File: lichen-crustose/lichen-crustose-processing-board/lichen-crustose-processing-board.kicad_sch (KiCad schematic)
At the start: 3 parts

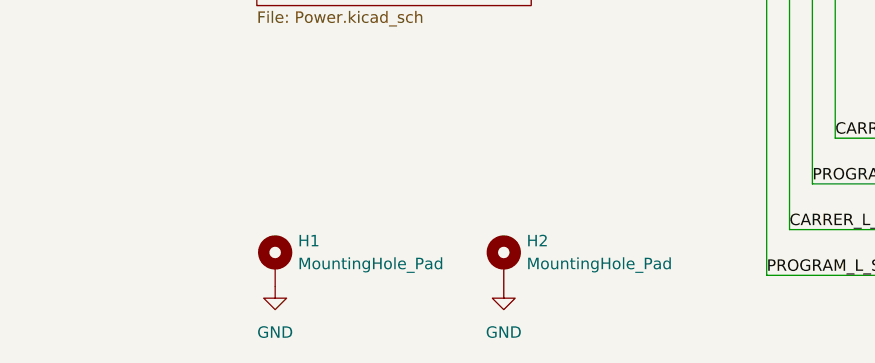
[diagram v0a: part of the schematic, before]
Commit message: Updates Lichen symbols and footprints. Fixes to Crustose and Vactrol VCA. Adds 3D model of the RP2350 dual USB board.
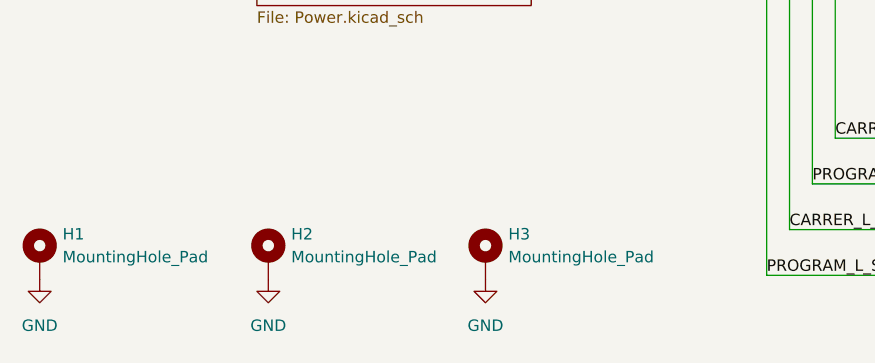
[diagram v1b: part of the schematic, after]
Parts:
- added H3: MountingHole_Pad, MountingHole:MountingHole_2.2mm_M2_Pad, symbol Mechanical:MountingHole_Pad
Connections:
- net GND: now also H3.1
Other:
- moved on the sheet: H1, H2
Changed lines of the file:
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@@
 	(symbol
 		(lib_id "power:GND")
-		(at 113.792 135.382 0)
+		(at 111.76 134.62 0)
 		(mirror y)
 		(unit 1)
@@
 		(dnp no)
 		(fields_autoplaced yes)
+		(property "Reference" "#PWR020"
+			(at 111.76 140.97 0)
+			(effects
+				(font
+					(size 1.27 1.27)
+				)
+				(hide yes)
+			)
+		)
+		(property "Value" "GND"
+			(at 111.76 139.7 0)
+			(effects
+				(font
+					(size 1.27 1.27)
+				)
+			)
+		)
+		(property "Footprint" ""
+			(at 111.76 134.62 0)
+			(effects
+				(font
+					(size 1.27 1.27)
+				)
+				(hide yes)
+			)
+		)
+		(property "Datasheet" ""
+			(at 111.76 134.62 0)
+			(effects
+				(font
+					(size 1.27 1.27)
+				)
+				(hide yes)
+			)
+		)
+		(property "Description" "Power symbol creates a global label with name \"GND\" , ground"
+			(at 111.76 134.62 0)
+			(effects
+				(font
+					(size 1.27 1.27)
+				)
+				(hide yes)
+			)
+		)
+		(pin "1"
+		)
+		(instances
+			(project "lichen-crustose-processing-board"
+				(path "/c32352bf-fefd-4f63-8ef8-68bcf6fd3821"
+					(reference "#PWR020")
+					(unit 1)
+				)
+			)
+		)
+	)
+	(symbol
+		(lib_id "power:GND")
+		(at 87.63 134.62 0)
+		(mirror y)
+		(unit 1)
+		(exclude_from_sim no)
+		(in_bom yes)
+		(on_board yes)
+		(dnp no)
+		(fields_autoplaced yes)
 		(property "Reference" "#PWR02"
-			(at 113.792 141.732 0)
+			(at 87.63 140.97 0)
 			(effects
 				(font
@@
 		)
 		(property "Value" "GND"
-			(at 113.792 140.462 0)
+			(at 87.63 139.7 0)
 			(effects
 				(font
@@
 		)
 		(property "Footprint" ""
-			(at 113.792 135.382 0)
+			(at 87.63 134.62 0)
 			(effects
 				(font
@@
 		)
 		(property "Datasheet" ""
-			(at 113.792 135.382 0)
+			(at 87.63 134.62 0)
 			(effects
 				(font
@@
 		)
 		(property "Description" "Power symbol creates a global label with name \"GND\" , ground"
-			(at 113.792 135.382 0)
+			(at 87.63 134.62 0)
 			(effects
 				(font
@@
 	)
 	(symbol
+		(lib_id "Mechanical:MountingHole_Pad")
+		(at 111.76 132.08 0)
+		(unit 1)
+		(exclude_from_sim no)
+		(in_bom no)
+		(on_board yes)
+		(dnp no)
+		(fields_autoplaced yes)
+		(property "Reference" "H3"
+			(at 114.3 129.5399 0)
+			(effects
+				(font
+					(size 1.27 1.27)
+				)
+				(justify left)
+			)
+		)
+		(property "Value" "MountingHole_Pad"
+			(at 114.3 132.0799 0)
+			(effects
+				(font
+					(size 1.27 1.27)
+				)
+				(justify left)
+			)
+		)
+		(property "Footprint" "MountingHole:MountingHole_2.2mm_M2_Pad"
+			(at 111.76 132.08 0)
+			(effects
+				(font
+					(size 1.27 1.27)
+				)
+				(hide yes)
+			)
+		)
+		(property "Datasheet" "~"
+			(at 111.76 132.08 0)
+			(effects
+				(font
+					(size 1.27 1.27)
+				)
+				(hide yes)
+			)
+		)
+		(property "Description" "Mounting Hole with connection"
+			(at 111.76 132.08 0)
+			(effects
+				(font
+					(size 1.27 1.27)
+				)
+				(hide yes)
+			)
+		)
+		(pin "1"
+		)
+		(instances
+			(project "lichen-crustose-processing-board"
+				(path "/c32352bf-fefd-4f63-8ef8-68bcf6fd3821"
+					(reference "H3")
+					(unit 1)
+				)
+			)
+		)
+	)
+	(symbol
 		(lib_id "power:GND")
-		(at 88.392 135.382 0)
+		(at 62.23 134.62 0)
 		(mirror y)
 		(unit 1)
@@
 		(fields_autoplaced yes)
 		(property "Reference" "#PWR01"
-			(at 88.392 141.732 0)
+			(at 62.23 140.97 0)
 			(effects
 				(font
@@
 		)
 		(property "Value" "GND"
-			(at 88.392 140.462 0)
+			(at 62.23 139.7 0)
 			(effects
 				(font
@@
 		)
 		(property "Footprint" ""
-			(at 88.392 135.382 0)
+			(at 62.23 134.62 0)
 			(effects
 				(font
@@
 		)
 		(property "Datasheet" ""
-			(at 88.392 135.382 0)
+			(at 62.23 134.62 0)
 			(effects
 				(font
@@
 		)
 		(property "Description" "Power symbol creates a global label with name \"GND\" , ground"
-			(at 88.392 135.382 0)
+			(at 62.23 134.62 0)
 			(effects
 				(font
@@
 	(symbol
 		(lib_id "Mechanical:MountingHole_Pad")
-		(at 88.392 132.842 0)
+		(at 62.23 132.08 0)
 		(unit 1)
 		(exclude_from_sim no)
@@
 		(fields_autoplaced yes)
 		(property "Reference" "H1"
-			(at 90.932 130.3019 0)
+			(at 64.77 129.5399 0)
 			(effects
 				(font
@@
 		)
 		(property "Value" "MountingHole_Pad"
-			(at 90.932 132.8419 0)
+			(at 64.77 132.0799 0)
 			(effects
 				(font
@@
 		)
 		(property "Footprint" "MountingHole:MountingHole_2.2mm_M2_Pad"
-			(at 88.392 132.842 0)
+			(at 62.23 132.08 0)
 			(effects
 				(font
@@
 		)
 		(property "Datasheet" "~"
-			(at 88.392 132.842 0)
+			(at 62.23 132.08 0)
 			(effects
 				(font
@@
 		)
 		(property "Description" "Mounting Hole with connection"
-			(at 88.392 132.842 0)
+			(at 62.23 132.08 0)
 			(effects
 				(font
@@
 	(symbol
 		(lib_id "Mechanical:MountingHole_Pad")
-		(at 113.792 132.842 0)
+		(at 87.63 132.08 0)
 		(unit 1)
 		(exclude_from_sim no)
@@
 		(fields_autoplaced yes)
 		(property "Reference" "H2"
-			(at 116.332 130.3019 0)
+			(at 90.17 129.5399 0)
 			(effects
 				(font
@@
 		)
 		(property "Value" "MountingHole_Pad"
-			(at 116.332 132.8419 0)
+			(at 90.17 132.0799 0)
 			(effects
 				(font
@@
 		)
 		(property "Footprint" "MountingHole:MountingHole_2.2mm_M2_Pad"
-			(at 113.792 132.842 0)
+			(at 87.63 132.08 0)
 			(effects
 				(font
@@
 		)
 		(property "Datasheet" "~"
-			(at 113.792 132.842 0)
+			(at 87.63 132.08 0)
 			(effects
 				(font
@@
 		)
 		(property "Description" "Mounting Hole with connection"
-			(at 113.792 132.842 0)
-			(effects
-				(font
+			(at 87.63 132.08 0)
+			(effects
+				(font
